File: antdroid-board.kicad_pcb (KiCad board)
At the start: 2 copper layers, 99.4 x 53.7 mm, 58 parts, among them P1 CONN_01X01, P2 CONN_01X01, Q1 BSS138, Q2 BSS138, U1 LM2678T-5.0, U2 LM2678T-5.0, U3 LM2675M-5

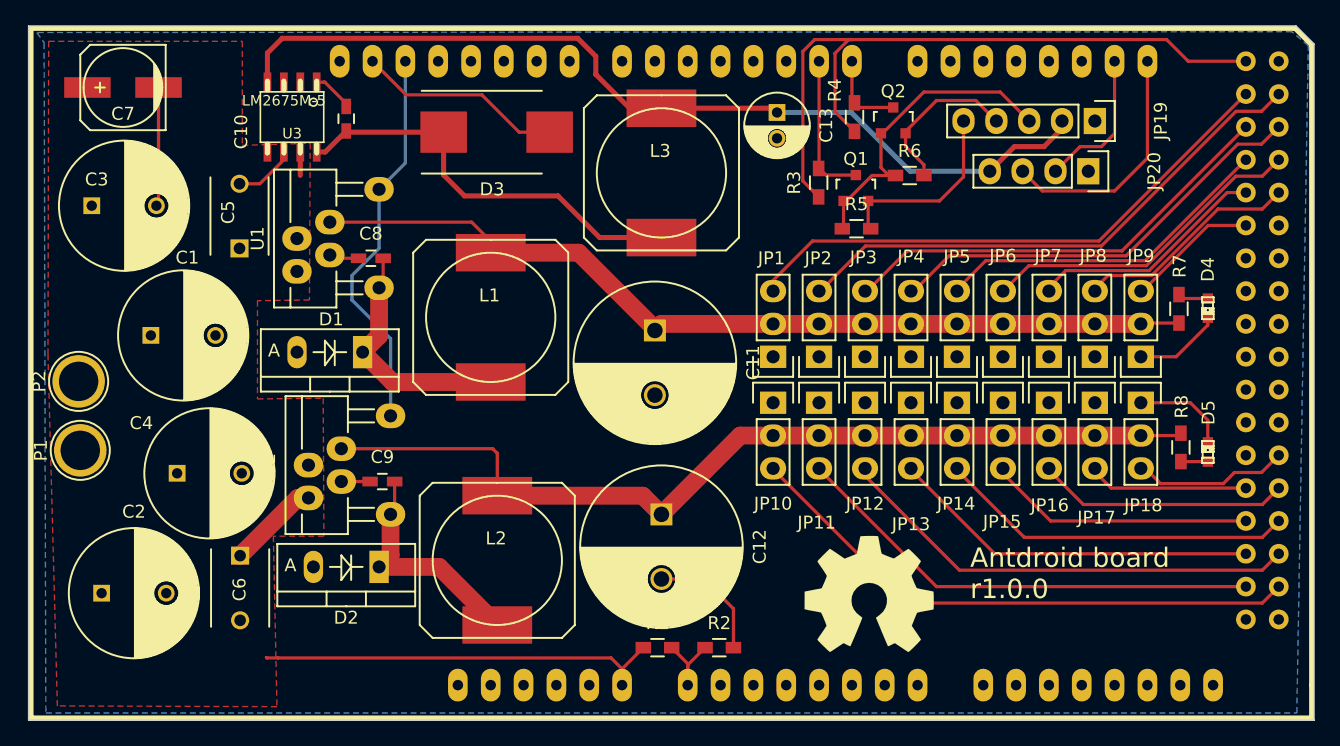
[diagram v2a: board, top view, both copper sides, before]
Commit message: Relocate libs and footprints
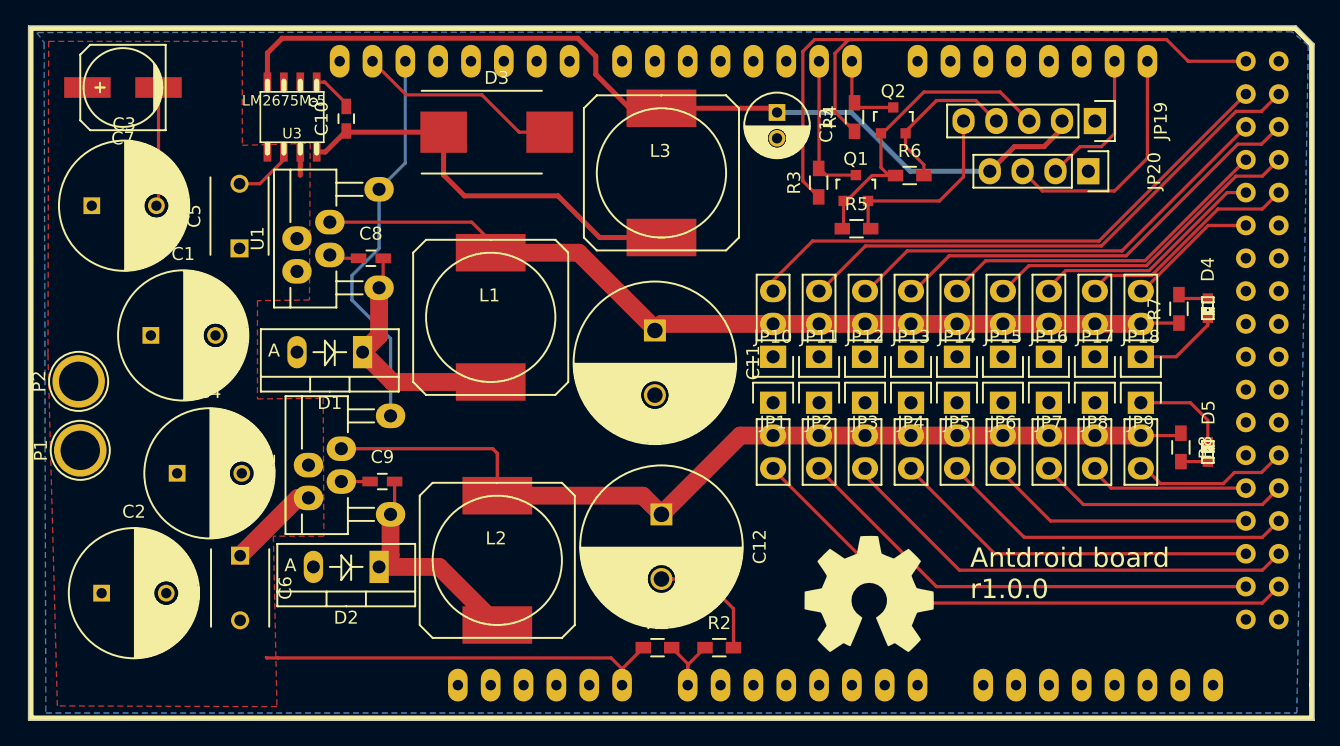
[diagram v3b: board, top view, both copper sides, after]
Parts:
- C1, C2, C3, C4: footprint Capacitors_ThroughHole:C_Radial_D10_L13_P5 -> antdroid-board:C_Radial_D10_L13_P5
- C10, C8, C9: footprint Capacitors_SMD:C_0603_HandSoldering -> antdroid-board:C_0603_HandSoldering
- C11, C12: footprint Capacitors_ThroughHole:C_Radial_D12.5_L25_P5 -> antdroid-board:C_Radial_D12.5_L25_P5
- C13: footprint Capacitors_ThroughHole:C_Radial_D5_L11_P2 -> antdroid-board:C_Radial_D5_L11_P2
- C5, C6: footprint Capacitors_ThroughHole:C_Disc_D6_P5 -> antdroid-board:C_Disc_D6_P5
- C7: footprint Capacitors_SMD:c_elec_6.3x7.7 -> antdroid-board:c_elec_6.3x7.7
- D1, D2: footprint Diodes_ThroughHole:Diode_TO-220_Vertical -> antdroid-board:Diode_TO-220_Vertical
- D3: footprint Diodes_SMD:Diode-DO-214AB_Handsoldering -> antdroid-board:Diode-DO-214AB_Handsoldering
- JP1, JP10, JP11, JP12, JP13, JP14, JP15, JP16, JP17, JP18, JP2, JP3, JP4, JP5, JP6, JP7, JP8, JP9: footprint Pin_Headers:Pin_Header_Straight_1x03 -> antdroid-board:Pin_Header_Straight_1x03
- JP19: footprint Pin_Headers:Pin_Header_Straight_1x05 -> antdroid-board:Pin_Header_Straight_1x05
- JP20: footprint Pin_Headers:Pin_Header_Straight_1x04 -> antdroid-board:Pin_Header_Straight_1x04
- L1, L2, L3: footprint Inductors:SELF-WE-PD-XXL -> antdroid-board:SELF-WE-PD-XXL
- P1, P2: footprint Connect:1pin -> antdroid-board:1pin
- Q1, Q2: footprint Housings_SOT-23_SOT-143_TSOT-6:SOT-23 -> antdroid-board:SOT-23
- R1, R2, R3, R4, R5, R6, R7, R8: footprint Resistors_SMD:R_0603_HandSoldering -> antdroid-board:R_0603_HandSoldering
- U1, U2: footprint Power_Integrations:TO-220-7C -> antdroid-board:TO-220-7C
- U3: footprint ab2_so:AB2_SO08 -> antdroid-board:AB2_SO08
